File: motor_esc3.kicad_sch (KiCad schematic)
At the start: 12 parts, among them U3 MCF8316A

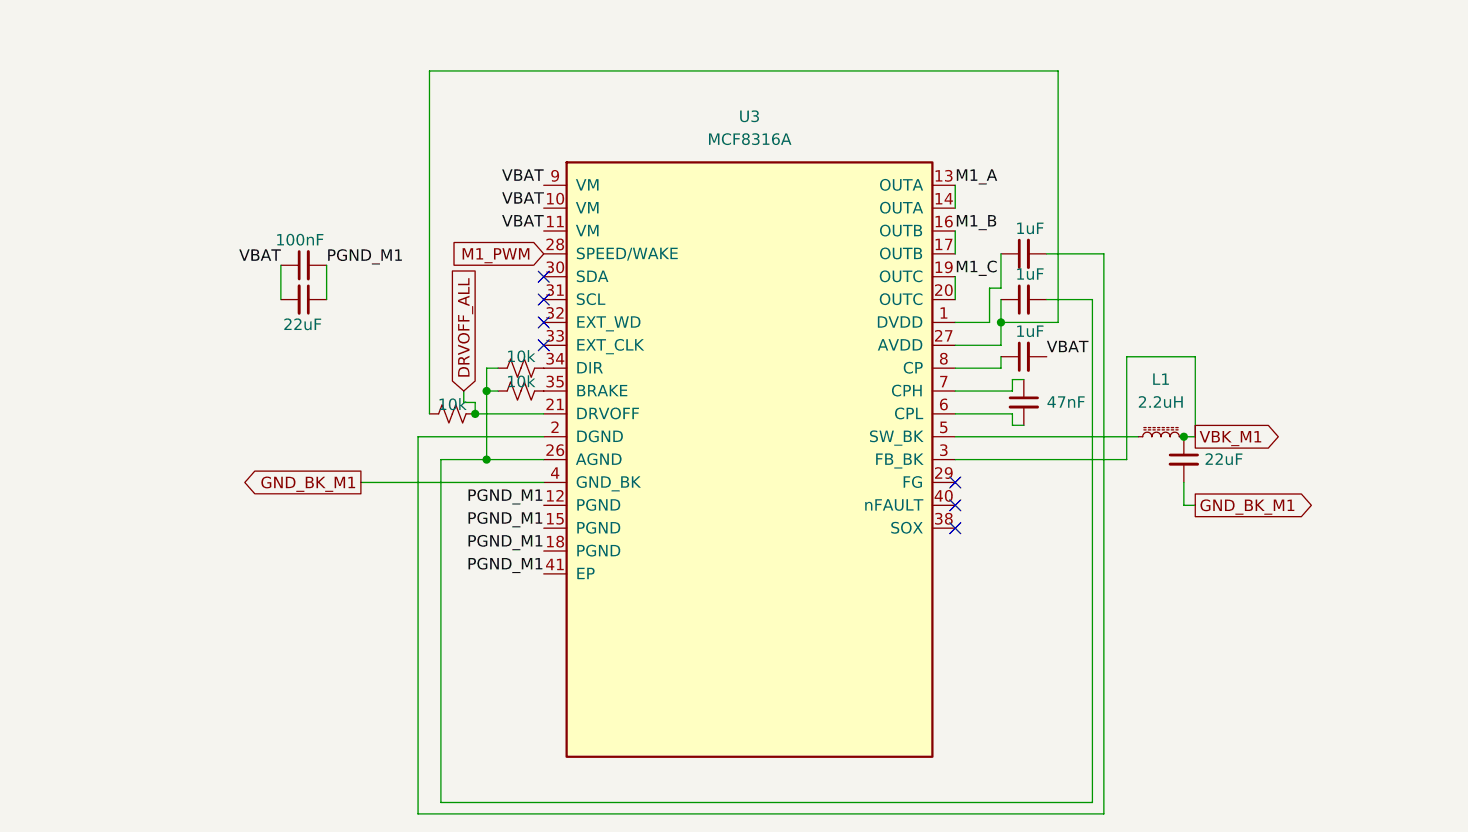
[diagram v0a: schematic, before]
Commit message: Schematics mostly done, netclasses, coords for esc (angled)
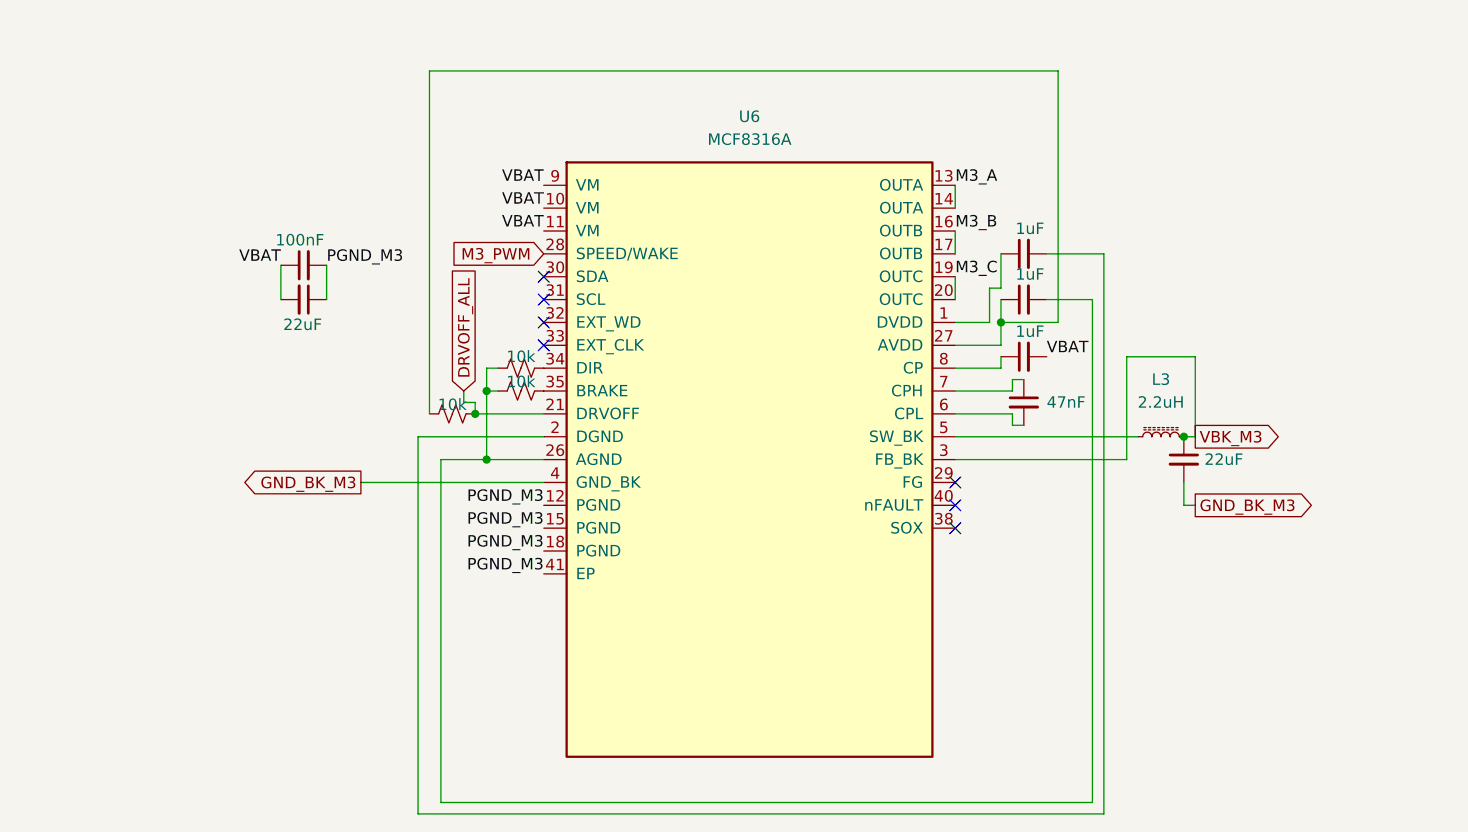
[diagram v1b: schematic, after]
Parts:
- U6: renamed from U3; footprint (none) -> MCF8316:MCF8316A_RGF0040E_VQFN-40-1EP_7x5mm_P0.5mm_EP5.5x3.5mm_kicad5_fixed_rotation
- renumbered C11 to C28, C10 to C29, C15 to C30, C14 to C31, C13 to C32, C12 to C33, C16 to C34, L1 to L3, R6 to R10, R4 to R11, R5 to R12
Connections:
- net GND_BK_M1 renamed GND_BK_M3
- net M1_A renamed M3_A
- net M1_B renamed M3_B
- net M1_C renamed M3_C
- net M1_PWM renamed M3_PWM
- net PGND_M1 renamed PGND_M3
- net VBK_M1 renamed VBK_M3
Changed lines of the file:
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@@
 		)
 	)
-	(label "PGND_M1"
+	(label "PGND_M3"
 		(at 109.22 92.71 180)
 		(effects
@@
 		)
 	)
-	(label "PGND_M1"
+	(label "PGND_M3"
 		(at 109.22 90.17 180)
 		(effects
@@
 		)
 	)
-	(label "PGND_M1"
+	(label "PGND_M3"
 		(at 109.22 95.25 180)
 		(effects
@@
 		)
 	)
-	(label "PGND_M1"
+	(label "PGND_M3"
 		(at 109.22 97.79 180)
 		(effects
@@
 		)
 	)
-	(label "PGND_M1"
+	(label "PGND_M3"
 		(at 85.09 63.5 0)
 		(effects
@@
 		)
 	)
-	(label "M1_C"
+	(label "M3_C"
 		(at 154.94 64.77 0)
 		(effects
@@
 		)
 	)
-	(label "M1_B"
+	(label "M3_B"
 		(at 154.94 59.69 0)
 		(effects
@@
 		)
 	)
-	(label "M1_A"
+	(label "M3_A"
 		(at 154.94 54.61 0)
 		(effects
@@
 		)
 	)
-	(global_label "GND_BK_M1"
+	(global_label "GND_BK_M3"
 		(shape output)
 		(at 88.9 87.63 180)
@@
 		)
 	)
-	(global_label "M1_PWM"
+	(global_label "M3_PWM"
 		(shape input)
 		(at 109.22 62.23 180)
@@
 		)
 	)
-	(global_label "VBK_M1"
+	(global_label "VBK_M3"
 		(shape output)
 		(at 181.61 82.55 0)
@@
 		)
 	)
-	(global_label "GND_BK_M1"
+	(global_label "GND_BK_M3"
 		(shape output)
 		(at 181.61 90.17 0)
@@
 		(on_board yes)
 		(dnp no)
-		(property "Reference" "C16"
+		(property "Reference" "C34"
 			(at 182.88 83.8262 0)
 			(effects
@@
 		(instances
 			(project "neodrone-v1"
-				(path "/ec430d83-72cd-4950-a197-fb5338d7c552/b94dd048-e648-4a17-b37c-6f29cafaf69f"
-					(reference "C16")
+				(path "/ec430d83-72cd-4950-a197-fb5338d7c552/8e4317d2-4bd9-4cda-9d68-812eca0aa468"
+					(reference "C34")
 					(unit 1)
 				)
@@
 		(on_board yes)
 		(dnp no)
-		(property "Reference" "R6"
+		(property "Reference" "R10"
 			(at 99.06 73.66 90)
 			(effects
@@
 		(instances
 			(project "neodrone-v1"
-				(path "/ec430d83-72cd-4950-a197-fb5338d7c552/b94dd048-e648-4a17-b37c-6f29cafaf69f"
-					(reference "R6")
+				(path "/ec430d83-72cd-4950-a197-fb5338d7c552/8e4317d2-4bd9-4cda-9d68-812eca0aa468"
+					(reference "R10")
 					(unit 1)
 				)
@@
 		(dnp no)
 		(fields_autoplaced yes)
-		(property "Reference" "L1"
+		(property "Reference" "L3"
 			(at 177.8 76.2 90)
 			(effects
@@
 		)
 		(instances
-			(project ""
-				(path "/ec430d83-72cd-4950-a197-fb5338d7c552/b94dd048-e648-4a17-b37c-6f29cafaf69f"
-					(reference "L1")
+			(project "neodrone-v1"
+				(path "/ec430d83-72cd-4950-a197-fb5338d7c552/8e4317d2-4bd9-4cda-9d68-812eca0aa468"
+					(reference "L3")
 					(unit 1)
 				)
@@
 		(on_board yes)
 		(dnp no)
-		(property "Reference" "C12"
+		(property "Reference" "C33"
 			(at 165.1 77.4762 0)
 			(effects
@@
 		(instances
 			(project "neodrone-v1"
-				(path "/ec430d83-72cd-4950-a197-fb5338d7c552/b94dd048-e648-4a17-b37c-6f29cafaf69f"
-					(reference "C12")
+				(path "/ec430d83-72cd-4950-a197-fb5338d7c552/8e4317d2-4bd9-4cda-9d68-812eca0aa468"
+					(reference "C33")
 					(unit 1)
 				)
@@
 		(dnp no)
 		(fields_autoplaced yes)
-		(property "Reference" "U3"
+		(property "Reference" "U6"
 			(at 132.08 46.99 0)
 			(effects
@@
 			)
 		)
-		(property "Footprint" ""
+		(property "Footprint" "MCF8316:MCF8316A_RGF0040E_VQFN-40-1EP_7x5mm_P0.5mm_EP5.5x3.5mm_kicad5_fixed_rotation"
 			(at 132.08 85.09 0)
 			(effects
@@
 		)
 		(instances
-			(project ""
-				(path "/ec430d83-72cd-4950-a197-fb5338d7c552/b94dd048-e648-4a17-b37c-6f29cafaf69f"
-					(reference "U3")
+			(project "neodrone-v1"
+				(path "/ec430d83-72cd-4950-a197-fb5338d7c552/8e4317d2-4bd9-4cda-9d68-812eca0aa468"
+					(reference "U6")
 					(unit 1)
 				)
@@
 		(on_board yes)
 		(dnp no)
-		(property "Reference" "C15"
+		(property "Reference" "C30"
 			(at 161.2962 59.69 0)
 			(effects
@@
 		(instances
 			(project "neodrone-v1"
-				(path "/ec430d83-72cd-4950-a197-fb5338d7c552/b94dd048-e648-4a17-b37c-6f29cafaf69f"
-					(reference "C15")
+				(path "/ec430d83-72cd-4950-a197-fb5338d7c552/8e4317d2-4bd9-4cda-9d68-812eca0aa468"
+					(reference "C30")
 					(unit 1)
 				)
@@
 		(on_board yes)
 		(dnp no)
-		(property "Reference" "R5"
+		(property "Reference" "R12"
 			(at 106.68 71.12 90)
 			(effects
@@
 		(instances
 			(project "neodrone-v1"
-				(path "/ec430d83-72cd-4950-a197-fb5338d7c552/b94dd048-e648-4a17-b37c-6f29cafaf69f"
-					(reference "R5")
+				(path "/ec430d83-72cd-4950-a197-fb5338d7c552/8e4317d2-4bd9-4cda-9d68-812eca0aa468"
+					(reference "R12")
 					(unit 1)
 				)
@@
 		(on_board yes)
 		(dnp no)
-		(property "Reference" "C14"
+		(property "Reference" "C31"
 			(at 161.2962 64.77 0)
 			(effects
@@
 		(instances
 			(project "neodrone-v1"
-				(path "/ec430d83-72cd-4950-a197-fb5338d7c552/b94dd048-e648-4a17-b37c-6f29cafaf69f"
-					(reference "C14")
+				(path "/ec430d83-72cd-4950-a197-fb5338d7c552/8e4317d2-4bd9-4cda-9d68-812eca0aa468"
+					(reference "C31")
 					(unit 1)
 				)
@@
 		(on_board yes)
 		(dnp no)
-		(property "Reference" "R4"
+		(property "Reference" "R11"
 			(at 106.68 68.58 90)
 			(effects
@@
 		(instances
 			(project "neodrone-v1"
-				(path "/ec430d83-72cd-4950-a197-fb5338d7c552/b94dd048-e648-4a17-b37c-6f29cafaf69f"
-					(reference "R4")
+				(path "/ec430d83-72cd-4950-a197-fb5338d7c552/8e4317d2-4bd9-4cda-9d68-812eca0aa468"
+					(reference "R11")
 					(unit 1)
 				)
@@
 		(on_board yes)
 		(dnp no)
-		(property "Reference" "C10"
+		(property "Reference" "C29"
 			(at 83.8138 69.85 0)
 			(effects
@@
 		(instances
 			(project "neodrone-v1"
-				(path "/ec430d83-72cd-4950-a197-fb5338d7c552/b94dd048-e648-4a17-b37c-6f29cafaf69f"
-					(reference "C10")
+				(path "/ec430d83-72cd-4950-a197-fb5338d7c552/8e4317d2-4bd9-4cda-9d68-812eca0aa468"
+					(reference "C29")
 					(unit 1)
 				)
@@
 		(on_board yes)
 		(dnp no)
-		(property "Reference" "C13"
+		(property "Reference" "C32"
 			(at 161.2962 71.12 0)
 			(effects
@@
 		(instances
 			(project "neodrone-v1"
-				(path "/ec430d83-72cd-4950-a197-fb5338d7c552/b94dd048-e648-4a17-b37c-6f29cafaf69f"
-					(reference "C13")
+				(path "/ec430d83-72cd-4950-a197-fb5338d7c552/8e4317d2-4bd9-4cda-9d68-812eca0aa468"
+					(reference "C32")
 					(unit 1)
 				)
@@
 		(on_board yes)
 		(dnp no)
-		(property "Reference" "C11"
+		(property "Reference" "C28"
 			(at 81.2862 60.96 0)
 			(effects
@@
 		(instances
 			(project "neodrone-v1"
-				(path "/ec430d83-72cd-4950-a197-fb5338d7c552/b94dd048-e648-4a17-b37c-6f29cafaf69f"
-					(reference "C11")
-					(unit 1)
-				)
+				(path "/ec430d83-72cd-4950-a197-fb5338d7c552/8e4317d2-4bd9-4cda-9d68-812eca0aa468"
+					(reference "C28")
+					(unit 1)
+				)

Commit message: A LOT of changes, current state is 2 of 4 ESCs routed, power revamped. \n Board almost done
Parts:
- removed R11: 10k, Resistor_SMD:R_0603_1608Metric_Pad0.98x0.95mm_HandSolder, symbol Device:R_Small_US
- added J10, J8, J9: SolderWirePad_1x01_SMD_3x6mm, Connector_Wire:SolderWirePad_1x01_SMD_3x6mm, symbol Connector:Conn_01x01_Pin
- U6: footprint MCF8316:MCF8316A_RGF0040E_VQFN-40-1EP_7x5mm_P0.5mm_EP5.5x3.5mm_kicad5_fixed_rotation -> MCF8316:MCF8316A_RGF0040E_VQFN-40-1EP_7x5mm_P0.5mm_EP5.5x3.5mm
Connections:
- net PGND_M3 is gone; now on net GND: C28.2, C29.1, U6.12 (PGND), U6.15 (PGND), U6.18 (PGND), U6.41 (EP)
- net M3_A: now also J8.1 (Pin_1)
- net M3_B: now also J9.1 (Pin_1)
- net M3_C: now also J10.1 (Pin_1)
- net at C31.1, U6.27 (AVDD): no longer R10.1
- net at C30.1, U6.1 (DVDD): now also R10.1
- net GND: now reaches C30.2, U6.2 (DGND)
- net GND: now also C31.2, R12.1, U6.26 (AGND)
- net at U6.34 (DIR): now also R12.2, U6.35 (BRAKE)

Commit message: done?
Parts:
- removed R10: 10k, Resistor_SMD:R_0603_1608Metric_Pad0.98x0.95mm_HandSolder, symbol Device:R_Small_US
- R12: footprint Resistor_SMD:R_0603_1608Metric_Pad0.98x0.95mm_HandSolder -> Resistor_SMD:R_0402_1005Metric_Pad0.72x0.64mm_HandSolder
